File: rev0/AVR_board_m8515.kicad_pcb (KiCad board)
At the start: 2 copper layers, 20.3 x 50.8 mm, 18 parts, among them IC1 ATMEGA8515-A, K1 SERIAL, P2 LEFT_HEADER, P3 CONN_3X2, P4 RIGHT_HEADER, P5 EXT_PWR, SW1 RESET_SW, X1 CRYSTAL_TH, X2 CRYSTAL_SMD

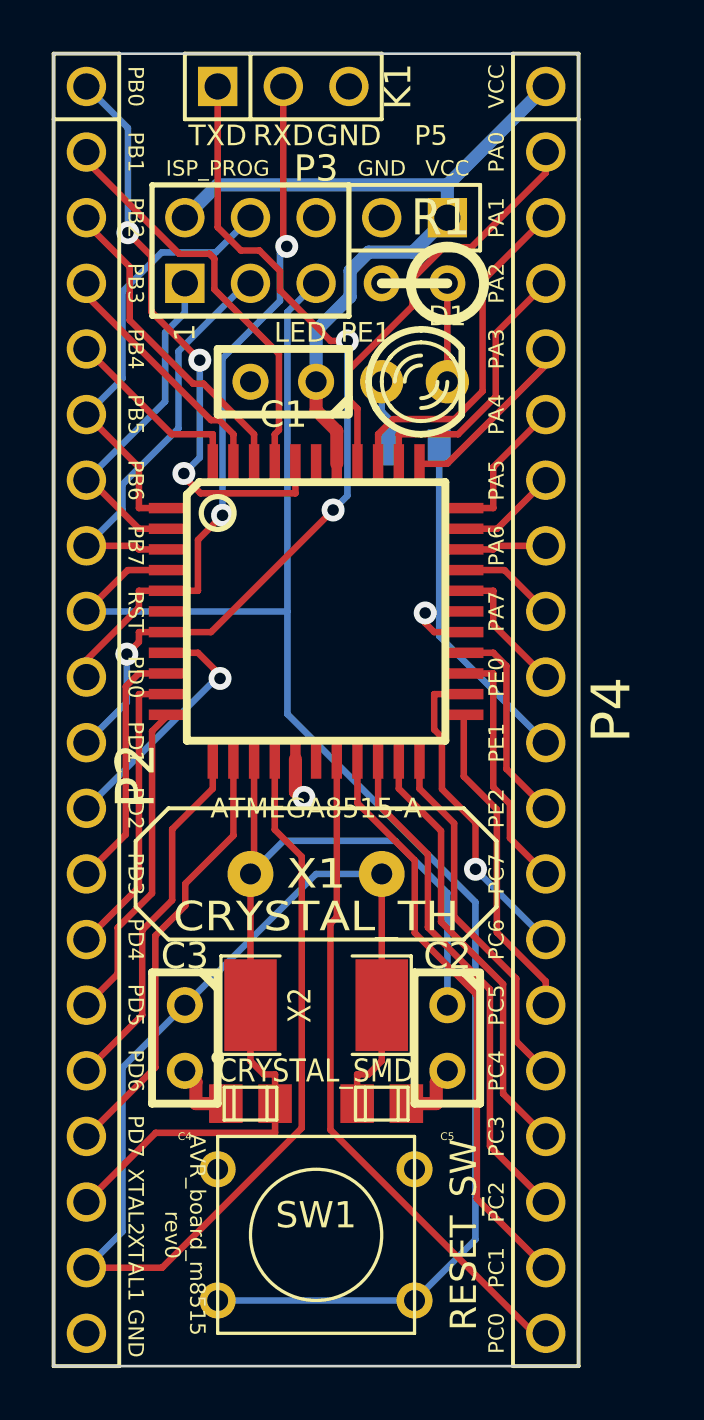
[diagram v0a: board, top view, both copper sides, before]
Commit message: fixed GND disconnects, will try to thicken the traces
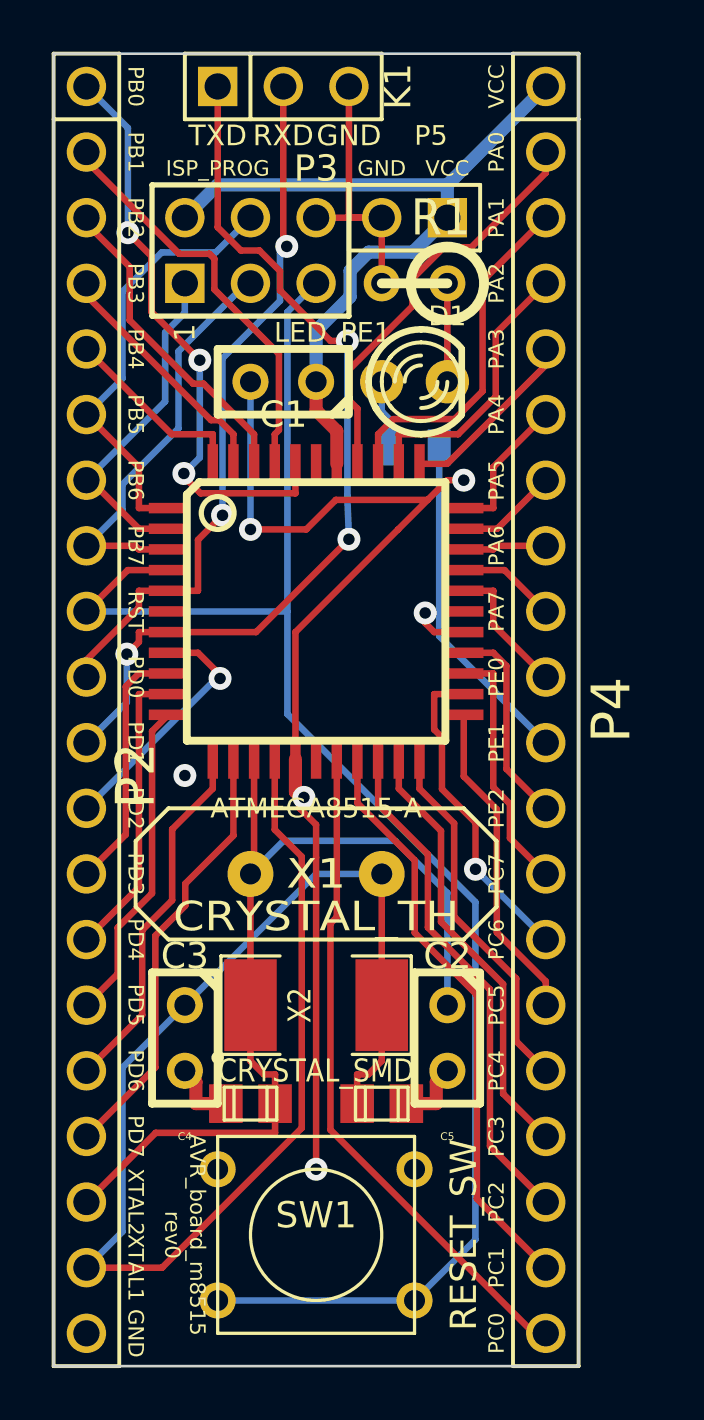
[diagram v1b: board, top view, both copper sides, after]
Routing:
- net GND: track 6.90 -> 60.0 mm, vias 1 -> 4
- net PD1: track 34.1 -> 35.2 mm
- net (no net): vias 0 -> 1
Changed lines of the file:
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@@
   (general
     (links 73)
-    (no_connects 6)
+    (no_connects 0)
     (area 135.560999 66.8528 158.559 119.709001)
     (thickness 1.6)
     (drawings 52)
-    (tracks 288)
+    (tracks 310)
     (zones 0)
     (modules 18)
@@
     (effects (font (size 0.8 0.8) (thickness 0.2)))
   )
+  (via (at 140.97 96.52) (size 0.889) (layers F.Cu B.Cu) (net 0))
+  (segment (start 150.368 85.852) (end 146.812 85.852) (width 0.254) (layer F.Cu) (net 1))
+  (via (at 143.51 86.995) (size 0.889) (layers F.Cu B.Cu) (net 1))
+  (segment (start 143.51 86.995) (end 143.51 81.28) (width 0.254) (layer B.Cu) (net 1))
+  (segment (start 145.669 86.995) (end 143.51 86.995) (width 0.254) (layer F.Cu) (net 1))
+  (segment (start 146.812 85.852) (end 145.669 86.995) (width 0.254) (layer F.Cu) (net 1))
+  (via (at 146.05 111.76) (size 0.889) (layers F.Cu B.Cu) (net 1))
+  (segment (start 145.5792 97.3677) (end 145.3668 97.1553) (width 0.508) (layer F.Cu) (net 1))
+  (segment (start 145.3668 97.1553) (end 145.2499 97.1553) (width 0.508) (layer F.Cu) (net 1))
+  (segment (start 145.2499 95.885) (end 145.2499 97.1553) (width 0.508) (layer F.Cu) (net 1))
   (via (at 145.5792 97.3677) (size 0.889) (layers F.Cu B.Cu) (net 1))
+  (segment (start 145.415 97.5319) (end 145.5792 97.3677) (width 0.254) (layer F.Cu) (net 1))
+  (segment (start 145.415 97.79) (end 145.415 97.5319) (width 0.254) (layer F.Cu) (net 1))
+  (segment (start 146.05 98.425) (end 145.415 97.79) (width 0.254) (layer F.Cu) (net 1))
+  (segment (start 146.05 99.695) (end 146.05 98.425) (width 0.254) (layer F.Cu) (net 1))
+  (segment (start 146.05 99.695) (end 146.05 111.76) (width 0.254) (layer F.Cu) (net 1))
+  (segment (start 151.765 85.09) (end 151.13 85.09) (width 0.254) (layer F.Cu) (net 1))
+  (via (at 151.765 85.09) (size 0.889) (layers F.Cu B.Cu) (net 1))
+  (segment (start 145.2499 90.9701) (end 145.2499 95.885) (width 0.254) (layer F.Cu) (net 1))
+  (segment (start 149.225 86.995) (end 145.2499 90.9701) (width 0.254) (layer F.Cu) (net 1))
+  (segment (start 150.368 85.852) (end 149.225 86.995) (width 0.254) (layer F.Cu) (net 1))
+  (segment (start 151.13 85.09) (end 150.368 85.852) (width 0.254) (layer F.Cu) (net 1))
+  (segment (start 148.59 74.93) (end 148.59 77.47) (width 0.254) (layer F.Cu) (net 1))
+  (segment (start 147.32 69.85) (end 147.32 74.93) (width 0.254) (layer F.Cu) (net 1))
+  (segment (start 147.32 74.93) (end 148.59 74.93) (width 0.254) (layer F.Cu) (net 1))
+  (segment (start 148.59 74.93) (end 146.05 74.93) (width 0.254) (layer F.Cu) (net 1))
   (segment (start 141.399 108.379) (end 141.399 109.22) (width 0.508) (layer F.Cu) (net 1))
   (segment (start 140.97 107.95) (end 141.399 108.379) (width 0.508) (layer F.Cu) (net 1))
@@
   (segment (start 151.13 107.95) (end 150.701 108.379) (width 0.508) (layer F.Cu) (net 1))
   (segment (start 149.5425 109.22) (end 150.701 109.22) (width 0.508) (layer F.Cu) (net 1))
-  (segment (start 145.2499 95.885) (end 145.2499 97.1553) (width 0.508) (layer F.Cu) (net 1))
-  (segment (start 145.3668 97.1553) (end 145.2499 97.1553) (width 0.508) (layer F.Cu) (net 1))
-  (segment (start 145.5792 97.3677) (end 145.3668 97.1553) (width 0.508) (layer F.Cu) (net 1))
   (segment (start 151.13 77.47) (end 151.13 81.28) (width 0.254) (layer F.Cu) (net 2))
   (segment (start 148.59 82.4227) (end 148.59 81.28) (width 0.254) (layer B.Cu) (net 3))
@@
   (segment (start 139.1917 90.0214) (end 137.16 92.0531) (width 0.254) (layer F.Cu) (net 28))
   (segment (start 139.1917 89.3699) (end 139.1917 90.0214) (width 0.254) (layer F.Cu) (net 28))
-  (via (at 146.7091 86.2446) (size 0.889) (layers F.Cu B.Cu) (net 29))
+  (via (at 147.32 87.376) (size 0.889) (layers F.Cu B.Cu) (net 29))
   (via (at 147.259 79.7007) (size 0.889) (layers F.Cu B.Cu) (net 29))
   (via (at 138.7242 91.8213) (size 0.889) (layers F.Cu B.Cu) (net 29))
-  (segment (start 141.9836 90.9701) (end 146.7091 86.2446) (width 0.254) (layer F.Cu) (net 29))
-  (segment (start 140.335 90.9701) (end 141.9836 90.9701) (width 0.254) (layer F.Cu) (net 29))
+  (segment (start 143.7259 90.9701) (end 147.32625 87.36975) (width 0.254) (layer F.Cu) (net 29))
+  (segment (start 140.335 90.9701) (end 143.7259 90.9701) (width 0.254) (layer F.Cu) (net 29) (status 400000))
   (segment (start 147.259 85.6947) (end 147.259 79.7007) (width 0.254) (layer B.Cu) (net 29))
-  (segment (start 146.7091 86.2446) (end 147.259 85.6947) (width 0.254) (layer B.Cu) (net 29))
+  (segment (start 147.32 87.376) (end 147.259 85.6947) (width 0.254) (layer B.Cu) (net 29))
   (segment (start 146.6117 79.7007) (end 147.259 79.7007) (width 0.254) (layer F.Cu) (net 29))
   (segment (start 144.6534 77.7424) (end 146.6117 79.7007) (width 0.254) (layer F.Cu) (net 29))

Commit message: change GND track width to 0.02 on most traces
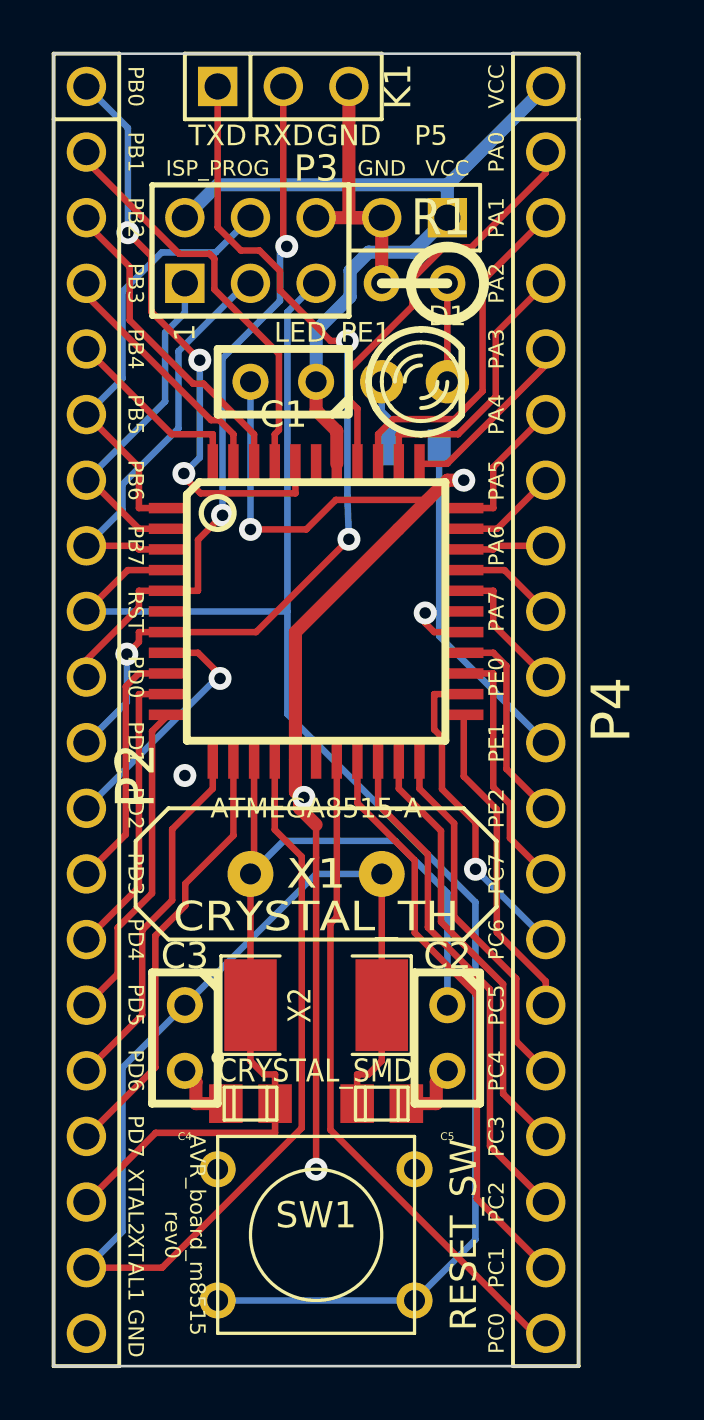
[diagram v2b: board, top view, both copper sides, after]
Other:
- net class gnd_stuff added: clearance 0.254, trace_width 0.508, via_dia 0.889, via_drill 0.635
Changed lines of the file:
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@@
     (uvia_drill 0.127)
     (add_net "")
-    (add_net GND)
     (add_net N-0000043)
     (add_net N-0000044)
@@
     (add_net XTAL1)
     (add_net XTAL2)
+  )
+  (net_class gnd_stuff ""
+    (clearance 0.254)
+    (trace_width 0.508)
+    (via_dia 0.889)
+    (via_drill 0.635)
+    (uvia_dia 0.508)
+    (uvia_drill 0.127)
+    (add_net GND)
   )
   (module C1 (layer F.Cu)
@@
   (segment (start 145.2499 95.885) (end 145.2499 97.1553) (width 0.508) (layer F.Cu) (net 1))
   (via (at 145.5792 97.3677) (size 0.889) (layers F.Cu B.Cu) (net 1))
-  (segment (start 145.415 97.5319) (end 145.5792 97.3677) (width 0.254) (layer F.Cu) (net 1))
-  (segment (start 145.415 97.79) (end 145.415 97.5319) (width 0.254) (layer F.Cu) (net 1))
-  (segment (start 146.05 98.425) (end 145.415 97.79) (width 0.254) (layer F.Cu) (net 1))
+  (segment (start 145.415 97.5319) (end 145.5792 97.3677) (width 0.508) (layer F.Cu) (net 1))
+  (segment (start 145.415 97.79) (end 145.415 97.5319) (width 0.508) (layer F.Cu) (net 1))
+  (segment (start 146.05 98.425) (end 145.415 97.79) (width 0.508) (layer F.Cu) (net 1))
   (segment (start 146.05 99.695) (end 146.05 98.425) (width 0.254) (layer F.Cu) (net 1))
   (segment (start 146.05 99.695) (end 146.05 111.76) (width 0.254) (layer F.Cu) (net 1))
-  (segment (start 151.765 85.09) (end 151.13 85.09) (width 0.254) (layer F.Cu) (net 1))
+  (segment (start 151.765 85.09) (end 151.13 85.09) (width 0.508) (layer F.Cu) (net 1))
+  (segment (start 151.13 85.09) (end 150.368 85.852) (width 0.508) (layer F.Cu) (net 1))
   (via (at 151.765 85.09) (size 0.889) (layers F.Cu B.Cu) (net 1))
-  (segment (start 145.2499 90.9701) (end 145.2499 95.885) (width 0.254) (layer F.Cu) (net 1))
-  (segment (start 149.225 86.995) (end 145.2499 90.9701) (width 0.254) (layer F.Cu) (net 1))
-  (segment (start 150.368 85.852) (end 149.225 86.995) (width 0.254) (layer F.Cu) (net 1))
-  (segment (start 151.13 85.09) (end 150.368 85.852) (width 0.254) (layer F.Cu) (net 1))
-  (segment (start 148.59 74.93) (end 148.59 77.47) (width 0.254) (layer F.Cu) (net 1))
-  (segment (start 147.32 69.85) (end 147.32 74.93) (width 0.254) (layer F.Cu) (net 1))
-  (segment (start 147.32 74.93) (end 148.59 74.93) (width 0.254) (layer F.Cu) (net 1))
-  (segment (start 148.59 74.93) (end 146.05 74.93) (width 0.254) (layer F.Cu) (net 1))
+  (segment (start 145.2499 90.9701) (end 145.2499 95.885) (width 0.508) (layer F.Cu) (net 1))
+  (segment (start 149.225 86.995) (end 145.2499 90.9701) (width 0.508) (layer F.Cu) (net 1))
+  (segment (start 150.368 85.852) (end 149.225 86.995) (width 0.508) (layer F.Cu) (net 1))
+  (segment (start 148.59 74.93) (end 148.59 77.47) (width 0.508) (layer F.Cu) (net 1))
+  (segment (start 147.32 69.85) (end 147.32 74.93) (width 0.508) (layer F.Cu) (net 1))
+  (segment (start 147.32 74.93) (end 148.59 74.93) (width 0.508) (layer F.Cu) (net 1))
+  (segment (start 148.59 74.93) (end 146.05 74.93) (width 0.508) (layer F.Cu) (net 1))
   (segment (start 141.399 108.379) (end 141.399 109.22) (width 0.508) (layer F.Cu) (net 1))
   (segment (start 140.97 107.95) (end 141.399 108.379) (width 0.508) (layer F.Cu) (net 1))

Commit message: trying to add more gnd trace connections
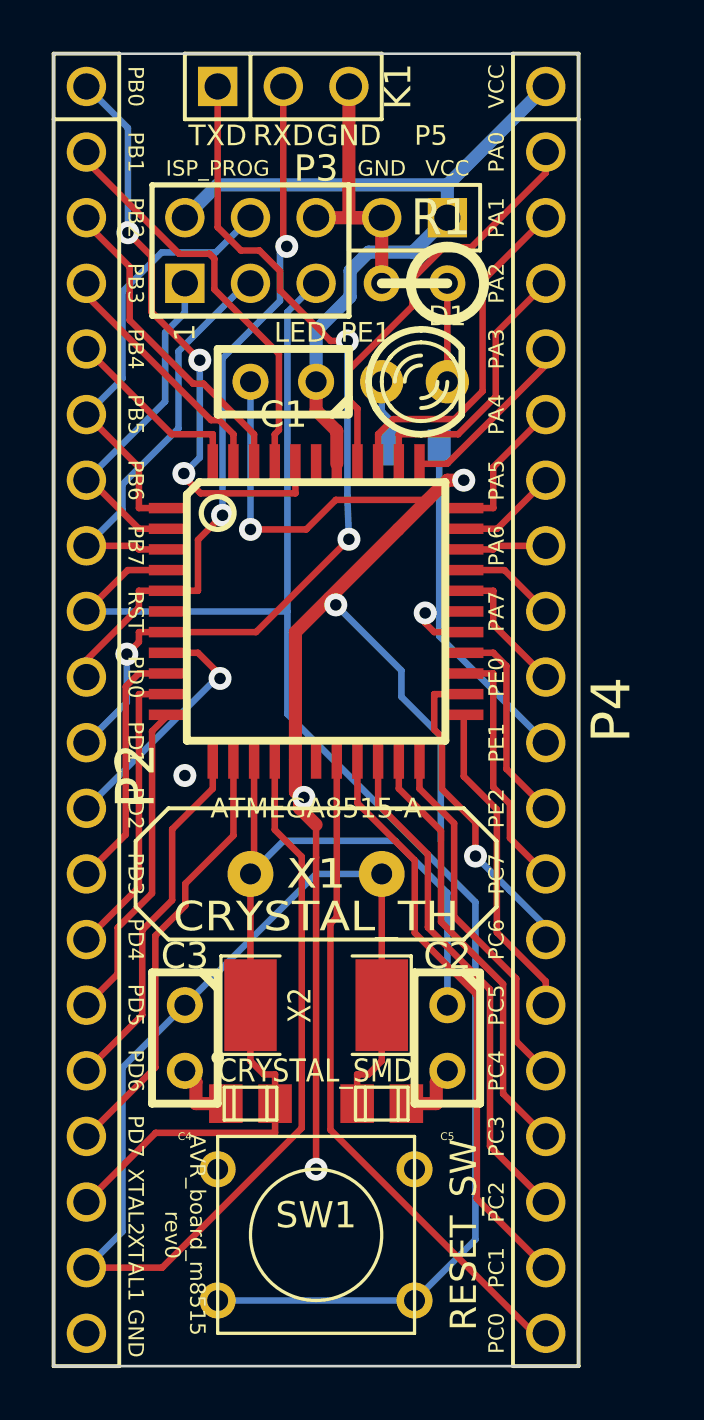
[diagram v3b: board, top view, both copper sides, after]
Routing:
- net GND: track 60.0 -> 71.2 mm, vias 4 -> 5
- net PC6: track 12.4 -> 11.9 mm
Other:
- net class gnd_stuff: clearance 0.254 -> 0.2032; trace_width 0.508 -> 0.254
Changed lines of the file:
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@@
     (thickness 1.6)
     (drawings 52)
-    (tracks 310)
+    (tracks 318)
     (zones 0)
     (modules 18)
@@
   )
   (net_class gnd_stuff ""
-    (clearance 0.254)
-    (trace_width 0.508)
+    (clearance 0.2032)
+    (trace_width 0.254)
     (via_dia 0.889)
     (via_drill 0.635)
@@
   )
   (via (at 140.97 96.52) (size 0.889) (layers F.Cu B.Cu) (net 0))
+  (segment (start 146.558 89.662) (end 146.812 89.916) (width 0.254) (layer F.Cu) (net 1))
+  (segment (start 150.876 94.996) (end 150.876 99.06) (width 0.254) (layer B.Cu) (net 1))
+  (segment (start 149.352 93.472) (end 150.876 94.996) (width 0.254) (layer B.Cu) (net 1))
+  (segment (start 149.352 92.456) (end 149.352 93.472) (width 0.254) (layer B.Cu) (net 1))
+  (segment (start 146.812 89.916) (end 149.352 92.456) (width 0.254) (layer B.Cu) (net 1))
+  (via (at 146.812 89.916) (size 0.889) (layers F.Cu B.Cu) (net 1))
   (segment (start 150.368 85.852) (end 146.812 85.852) (width 0.254) (layer F.Cu) (net 1))
   (via (at 143.51 86.995) (size 0.889) (layers F.Cu B.Cu) (net 1))
@@
   (segment (start 146.812 85.852) (end 145.669 86.995) (width 0.254) (layer F.Cu) (net 1))
   (via (at 146.05 111.76) (size 0.889) (layers F.Cu B.Cu) (net 1))
+  (segment (start 146.05 99.695) (end 146.05 111.76) (width 0.254) (layer F.Cu) (net 1))
+  (segment (start 146.05 99.695) (end 146.05 98.425) (width 0.254) (layer F.Cu) (net 1))
+  (segment (start 146.05 98.425) (end 145.415 97.79) (width 0.508) (layer F.Cu) (net 1))
+  (segment (start 145.415 97.79) (end 145.415 97.5319) (width 0.508) (layer F.Cu) (net 1))
+  (segment (start 145.415 97.5319) (end 145.5792 97.3677) (width 0.508) (layer F.Cu) (net 1))
+  (via (at 145.5792 97.3677) (size 0.889) (layers F.Cu B.Cu) (net 1))
+  (segment (start 145.2499 95.885) (end 145.2499 97.1553) (width 0.508) (layer F.Cu) (net 1))
+  (segment (start 145.3668 97.1553) (end 145.2499 97.1553) (width 0.508) (layer F.Cu) (net 1))
   (segment (start 145.5792 97.3677) (end 145.3668 97.1553) (width 0.508) (layer F.Cu) (net 1))
-  (segment (start 145.3668 97.1553) (end 145.2499 97.1553) (width 0.508) (layer F.Cu) (net 1))
-  (segment (start 145.2499 95.885) (end 145.2499 97.1553) (width 0.508) (layer F.Cu) (net 1))
-  (via (at 145.5792 97.3677) (size 0.889) (layers F.Cu B.Cu) (net 1))
-  (segment (start 145.415 97.5319) (end 145.5792 97.3677) (width 0.508) (layer F.Cu) (net 1))
-  (segment (start 145.415 97.79) (end 145.415 97.5319) (width 0.508) (layer F.Cu) (net 1))
-  (segment (start 146.05 98.425) (end 145.415 97.79) (width 0.508) (layer F.Cu) (net 1))
-  (segment (start 146.05 99.695) (end 146.05 98.425) (width 0.254) (layer F.Cu) (net 1))
-  (segment (start 146.05 99.695) (end 146.05 111.76) (width 0.254) (layer F.Cu) (net 1))
   (segment (start 151.765 85.09) (end 151.13 85.09) (width 0.508) (layer F.Cu) (net 1))
   (segment (start 151.13 85.09) (end 150.368 85.852) (width 0.508) (layer F.Cu) (net 1))
   (via (at 151.765 85.09) (size 0.889) (layers F.Cu B.Cu) (net 1))
   (segment (start 145.2499 90.9701) (end 145.2499 95.885) (width 0.508) (layer F.Cu) (net 1))
-  (segment (start 149.225 86.995) (end 145.2499 90.9701) (width 0.508) (layer F.Cu) (net 1))
+  (segment (start 149.225 86.995) (end 146.558 89.662) (width 0.508) (layer F.Cu) (net 1))
+  (segment (start 146.558 89.662) (end 145.2499 90.9701) (width 0.508) (layer F.Cu) (net 1))
   (segment (start 150.368 85.852) (end 149.225 86.995) (width 0.508) (layer F.Cu) (net 1))
   (segment (start 148.59 74.93) (end 148.59 77.47) (width 0.508) (layer F.Cu) (net 1))
@@
   (segment (start 154.94 104.4884) (end 153.0446 102.593) (width 0.254) (layer F.Cu) (net 25))
   (segment (start 154.94 105.41) (end 154.94 104.4884) (width 0.254) (layer F.Cu) (net 25))
-  (via (at 152.2188 100.1488) (size 0.889) (layers F.Cu B.Cu) (net 26))
+  (via (at 152.2188 99.6408) (size 0.889) (layers F.Cu B.Cu) (net 26))
   (segment (start 151.765 93.3704) (end 150.6217 93.3704) (width 0.254) (layer F.Cu) (net 26))
-  (segment (start 154.94 102.87) (end 152.2188 100.1488) (width 0.254) (layer B.Cu) (net 26))
-  (segment (start 152.2188 98.3439) (end 152.2188 100.1488) (width 0.254) (layer F.Cu) (net 26))
+  (segment (start 154.94 102.362) (end 153.543 100.965) (width 0.254) (layer B.Cu) (net 26))
+  (segment (start 153.543 100.965) (end 152.2188 99.6408) (width 0.254) (layer B.Cu) (net 26))
+  (segment (start 152.2188 98.3439) (end 152.2188 99.6408) (width 0.254) (layer F.Cu) (net 26))
   (segment (start 150.9217 97.0468) (end 152.2188 98.3439) (width 0.254) (layer F.Cu) (net 26))
   (segment (start 150.9217 95.0417) (end 150.9217 97.0468) (width 0.254) (layer F.Cu) (net 26))
@@
   (via (at 138.7242 91.8213) (size 0.889) (layers F.Cu B.Cu) (net 29))
   (segment (start 143.7259 90.9701) (end 147.32625 87.36975) (width 0.254) (layer F.Cu) (net 29))
-  (segment (start 140.335 90.9701) (end 143.7259 90.9701) (width 0.254) (layer F.Cu) (net 29) (status 400000))
+  (segment (start 140.335 90.9701) (end 143.7259 90.9701) (width 0.254) (layer F.Cu) (net 29))
   (segment (start 147.259 85.6947) (end 147.259 79.7007) (width 0.254) (layer B.Cu) (net 29))
   (segment (start 147.32 87.376) (end 147.259 85.6947) (width 0.254) (layer B.Cu) (net 29))
